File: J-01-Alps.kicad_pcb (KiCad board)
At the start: 2 copper layers, 184 parts, among them SW1 SW_Push, U1 ATmega32U4-AU, U4 PRTR5V0U2X, Y1 16MHz

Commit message: Footprint changes
Changed all of the MX+Alps footprints to Alps only. Also added MX Stabilizer footprints.
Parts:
- removed R6: 10k, Resistor_SMD:R_0603_1608Metric_Pad0.98x0.95mm_HandSolder
- added RC4: 10k, Resistor_SMD:R_0603_1608Metric_Pad0.98x0.95mm_HandSolder, B.Cu at (82.5, 115.0)
- added SW-3800CAPS1: MX_Alps-1.75U, Alps_Only:ALPS-1.5U, F.Cu at (89.7, 113.5)
- added Stab-225U1: Stab-2.25U, MX_Alps_Hybrid:MX-2.25U-Stab-Only, F.Cu at (339.7, 113.5)
- added Stab-225U2: Stab-2.25U, MX_Alps_Hybrid:MX-2.25U-Stab-Only, F.Cu at (96.8, 132.6)
- added Stab-2U1: Stab-2U, MX_Alps_Hybrid:MX-2U-Stab-Only, F.Cu at (342.1, 75.4)
- added Stab-625U1: Stab-6.25U, MX_Alps_Hybrid:MX-6.25U-Stab-Only-Reversed, F.Cu at (206.4, 151.6)
- added Stab-7U1: Stab-7U, MX_Alps_Hybrid:MX-7U-Stab-Only-Reversed, F.Cu at (199.2, 151.6)
- C2, C5, C6, C7, C8, CC1, CC2, D36, D37, D38, D39, D40, D41, D42, D43, D44, D45, D46, D47, D48, D49, D50, D51, D52, D53, D54, D55, D56, D57, D58, D59, D60, D61, D62, D63, D64, D65, D66, D67, D68, D69, D70, D71, D72, D73, D74, D75, D76, D77, D78, D79, D80, F1, JST2, RC1, RC2, RC3, SW1, U1, U4, Y1: moved to B.Cu
- SW-#1, SW-'1, SW-,1, SW--1, SW-.1, SW-/1, SW-0, SW-1, SW-2, SW-3, SW-4, SW-5, SW-6, SW-7, SW-8, SW-9, SW-;1, SW-=1, SW-A1, SW-B1, SW-C1, SW-D1, SW-DEL1, SW-DOWN1, SW-E1, SW-END1, SW-ESC1, SW-F1, SW-G1, SW-H1, SW-I1, SW-J1, SW-K1, SW-L1, SW-LEFT1, SW-M1, SW-M10, SW-M11, SW-M2, SW-M3, SW-M4, SW-M5, SW-M6, SW-M7, SW-M8, SW-M9, SW-N1, SW-O1, SW-P1, SW-PGDN1, SW-PGUP1, SW-Q1, SW-R1, SW-RIGHT1, SW-S1, SW-T1, SW-U1, SW-UP1, SW-V1, SW-W1, SW-X1, SW-Y1, SW-Z1, SW-[1, SW-\1, SW-\3, SW-]1, SW-`1: footprint MX_Alps_Hybrid:MX-1U-NoLED -> Alps_Only:ALPS-1U
- SW-ANSIEN1, SW-LSHIFT1: footprint MX_Alps_Hybrid:MX-2.25U-NoLED -> Alps_Only:ALPS-2.25U
- SW-BKSP1: footprint MX_Alps_Hybrid:MX-2U-NoLED -> Alps_Only:ALPS-2U
- SW-CAPS1, SW-RSHFT1: footprint MX_Alps_Hybrid:MX-1.75U-NoLED -> Alps_Only:ALPS-1.75U
- SW-ISOEN1: footprint MX_Alps_Hybrid:MX-ISO-ReversedStabilizers -> Alps_Only:ALPS-ISO-FLIPPED
- SW-LALT1, SW-LCTRL1, SW-LSHIFT2, SW-LWIN1, SW-STEPCAPS1: footprint MX_Alps_Hybrid:MX-1.25U-NoLED -> Alps_Only:ALPS-1.25U
- SW-LALT2, SW-LCTRL2, SW-RALT1, SW-RCTRL1, SW-TAB1, SW-\2: footprint MX_Alps_Hybrid:MX-1.5U-NoLED -> Alps_Only:ALPS-1.5U
- SW-SPACE625: footprint MX_Alps_Hybrid:MX-6.25U-ReversedStabilizers-NoLED -> Alps_Only:ALPS-6.25U
- SW-SPACE7: footprint MX_Alps_Hybrid:MX-7U-ReversedStabilizers-NoLED -> Alps_Only:ALPS-7U
- moved D70 218.1 mm to (42.9, 154.0), turned to 90 degrees
- moved D52 211.8 mm to (379.4, 115.9), turned to 90 degrees
- moved D71 198.8 mm to (61.9, 154.0), turned to 90 degrees
- moved D51 190.8 mm to (349.2, 114.3), turned to 90 degrees
- moved RC1 181.8 mm to (64.3, 84.1)
- moved RC2 181.4 mm to (64.3, 85.7)
- moved D37 175.9 mm to (60.3, 115.9), turned to 90 degrees
- moved D69 171.5 mm to (379.4, 134.9), turned to 90 degrees
- moved U4 170.9 mm to (70.6, 85.2), turned to 90 degrees
- moved D50 170.4 mm to (333.4, 115.9), turned to 90 degrees
- moved CC1 169.3 mm to (67.5, 93.6), turned to 270 degrees
- moved D72 168.8 mm to (92.1, 154.0), turned to 90 degrees
- moved D36 166.1 mm to (42.9, 115.9), turned to 90 degrees
- moved C2 165.6 mm to (64.3, 111.9), turned to 270 degrees
- moved F1 165.4 mm to (70.6, 80.2)
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
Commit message: Initial routing and additional switch footprints
More bottom row option support (6U, split spacebar), and the start of some column and row routing.
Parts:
- added D75: SOD-123, Diode_SMD:D_SOD-123, B.Cu at (177.0, 154.1)
- added D77: SOD-123, Diode_SMD:D_SOD-123, B.Cu at (269.9, 154.1)
- added SW-LALT3: MX_Alps-1.25U, Alps_Only:ALPS-1.25U, F.Cu at (130.2, 151.6)
- added SW-LALT4: MX_Alps-1.5U, Alps_Only:ALPS-1.5U, F.Cu at (137.3, 151.6)
- added SW-LWIN2: MX_Alps-1U, Alps_Only:ALPS-1U, F.Cu at (108.7, 151.6)
- added SW-LWIN3: MX_Alps-1.U, Alps_Only:ALPS-1U, F.Cu at (113.5, 151.6)
- added SW-MENU1: MX_Alps-1U, Alps_Only:ALPS-1U, F.Cu at (289.7, 151.6)
- added SW-MENU2: MX_Alps-1U, Alps_Only:ALPS-1U, F.Cu at (285.0, 151.6)
- added SW-RALT2: MX_Alps-1.25U, Alps_Only:ALPS-1.25U, F.Cu at (268.3, 151.6)
- added SW-RALT3: MX_Alps-1.5U, Alps_Only:ALPS-1.5U, F.Cu at (261.1, 151.6)
- added SW-RCTRL2: MX_Alps-1.25U, Alps_Only:ALPS-1.25U, F.Cu at (311.1, 151.6)
- added SW-SPACE225: MX_Alps-2.25U, Alps_Only:ALPS-2.25U, F.Cu at (173.0, 151.6)
- added SW-SPACE275: MX_Alps-2.75U, Alps_Only:ALPS-2.75U, F.Cu at (220.7, 151.6)
- added SW-SPACE6: MX_Alps-6U, MX_Alps_Hybrid:MX-6U-Centered-ReversedStabilizers-NoLED, F.Cu at (199.2, 151.6)
- added Stab-225U2: Stab-2.25U, MX_Alps_Hybrid:MX-2.25U-Stab-Only, F.Cu at (173.0, 151.6)
- added Stab-275U1: Stab-2.75U, MX_Alps_Hybrid:MX-2.75U-Stab-Only, F.Cu at (220.7, 151.6)
- moved D79 2.38 mm to (313.5, 154.0)
- moved D72 2.38 mm to (89.7, 154.0)
- moved C2 2.14 mm to (65.2, 110.0)
- moved F1 1.26 mm to (70.0, 81.2)
- moved RC1 1.02 mm to (65.2, 84.5)
- moved RC2 1.00 mm to (65.2, 86.0), turned to 180 degrees
- moved CC1 0.80 mm to (68.3, 93.7)
- moved CC2 0.80 mm to (77.0, 93.7)
- moved C5 0.79 mm to (69.1, 118.3)
- moved C6 0.79 mm to (78.6, 118.3)
- moved C8 0.73 mm to (71.2, 100.5)
- renumbered D75 to D76, D76 to D78, D77 to D79, D78 to D80, D79 to D81, D80 to D82, Stab-225U2 to Stab-225U3
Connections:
- SW-LALT2 pad 1: COL4 -> COL3
- SW-LALT2 pad 2: Net-(D74-Pad2) -> Net-(D73-Pad2)
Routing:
- net ROW0: track 0.00 -> 338.0 mm
- net COL8: track 0.00 -> 106.7 mm
- net COL15: track 0.00 -> 106.4 mm
- net COL3: track 0.00 -> 103.8 mm
- net COL2: track 0.00 -> 103.7 mm
- net D-: track 0.00 -> 100.0 mm, vias 0 -> 2
- net COL12: track 0.00 -> 98.8 mm
- net D+: track 0.00 -> 98.4 mm, vias 0 -> 2
- net COL11: track 0.00 -> 94.8 mm
- net COL13: track 0.00 -> 92.4 mm
- net COL4: track 0.00 -> 91.4 mm
- net COL6: track 0.00 -> 89.0 mm
- net COL16: track 0.00 -> 88.0 mm
- net COL17: track 0.00 -> 80.7 mm
- net COL1: track 0.00 -> 76.2 mm
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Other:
- board outline added: 354 x 96.8 mm
- net class Default: trace_width 0.25 -> 0.254
- net class Power added: clearance 0.2, trace_width 0.381, via_dia 0.8, via_drill 0.4

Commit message: Routing work continued
Most routes placed. Will need to be optimized and cleaned up, but most paths have been figured out.
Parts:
- moved CC2 11.1 mm to (66.0, 95.5), turned to 270 degrees
- moved D74 8.78 mm to (127.8, 154.0)
- moved CC1 5.74 mm to (73.7, 95.5), turned to 90 degrees
- moved D76 4.76 mm to (204.0, 154.0)
- moved Y1 3.35 mm to (69.9, 95.5), turned to 180 degrees
- moved D72 2.56 mm to (92.2, 154.0)
- moved D73 2.24 mm to (115.8, 154.0)
- moved C7 1.85 mm to (81.2, 103.4)
- moved D75 1.51 mm to (175.5, 154.1)
- moved C6 1.15 mm to (78.0, 117.2)
- moved RC3 1.12 mm to (69.6, 134.8)
- moved C5 1.09 mm to (69.5, 117.2)
- moved RC4 1.07 mm to (81.5, 114.8)
- moved D77 0.88 mm to (270.8, 154.1)
- moved D56 0.55 mm to (113.8, 134.9)
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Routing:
- net ROW3: track 0.00 -> 413.8 mm, vias 0 -> 2
- net ROW4: track 0.00 -> 400.9 mm, vias 0 -> 2
- net ROW2: track 0.00 -> 378.7 mm, vias 0 -> 2
- net ROW1: track 0.00 -> 347.2 mm, vias 0 -> 2
- net COL17: track 80.7 -> 388.9 mm
- net COL16: track 88.0 -> 378.4 mm, vias 0 -> 1
- net COL15: track 106.4 -> 385.8 mm
- net COL14: track 64.1 -> 317.6 mm
- net COL13: track 92.4 -> 325.8 mm
- net COL12: track 98.8 -> 312.0 mm
- net COL11: track 94.8 -> 284.0 mm
- net COL10: track 67.0 -> 242.0 mm
- net COL9: track 67.0 -> 222.9 mm
- net COL8: track 106.7 -> 243.8 mm
- net COL7: track 67.0 -> 184.7 mm
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- added copper zone on F.Cu, net +5V
- added copper zone on B.Cu, net GND

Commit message: Continued work on layout
Layout refinements, USB traces, etc.
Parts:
- U4: footprint Package_TO_SOT_SMD:SOT-143 -> random-keyboard-parts:SOT143B
- moved CC2 5.78 mm to (68.9, 90.5), turned to 90 degrees
- moved CC1 5.39 mm to (71.7, 90.5)
- moved JST2 2.77 mm to (75.8, 85.2)
- moved RC3 1.91 mm to (71.5, 134.8), turned to 180 degrees
- moved F1 1.58 mm to (68.5, 81.8)
- moved RC1 1.50 mm to (63.8, 84.5)
- moved RC2 1.50 mm to (63.8, 86.0)
- moved U4 1.50 mm to (69.1, 85.2)
- moved Y1 0.62 mm to (70.3, 95.1)
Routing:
- net +5V: track 29.7 -> 125.2 mm, vias 10 -> 9
- net GND: track 57.0 -> 93.9 mm, vias 0 -> 17
- net ROW4: track 400.9 -> 421.7 mm
- net COL17: track 388.9 -> 408.9 mm
- net COL16: track 378.4 -> 390.7 mm
- net ROW0: track 376.5 -> 385.4 mm, vias 2 -> 0
- net Net-(JST2-Pad2): track 4.61 -> 10.1 mm
- net ROW1: track 347.2 -> 352.6 mm
- net Net-(JST2-Pad3): track 4.73 -> 10.1 mm
- net COL13: track 325.8 -> 330.2 mm
- net COL14: track 317.6 -> 322.0 mm
- net XTAL1: track 11.0 -> 15.3 mm
- net VCC: track 2.93 -> 6.62 mm
- net XTAL2: track 15.5 -> 19.1 mm
- net COL15: track 385.8 -> 389.3 mm
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- added copper zone on F.Cu, net GND
- removed copper zone on F.Cu, net +5V
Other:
- board size 354 x 96.8 mm -> 354.6 x 97.3 mm

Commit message: Verification of routing and dimension
Finished verifying the routing is correct, and the edge-cut dimensions are correct. Double checked the separation between switch areas for Macro columns and arrows / 65% extension keys. Added renders.
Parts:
- moved D69 3.29 mm to (382.7, 134.9)
- moved D18 3.29 mm to (382.7, 77.8)
- moved D35 3.29 mm to (382.7, 96.8)
- moved D52 3.29 mm to (382.7, 115.9)
- moved SW-M1 3.18 mm to (37.3, 75.4)
- moved SW-M3 3.18 mm to (37.3, 94.5)
- moved SW-M5 3.18 mm to (37.3, 113.5)
- moved SW-M2 3.18 mm to (56.4, 75.4)
- moved SW-M4 3.18 mm to (56.4, 94.5)
- moved SW-M6 3.18 mm to (56.4, 113.5)
- moved D2 3.18 mm to (58.7, 77.8)
- moved D20 3.18 mm to (58.7, 96.8)
- moved D54 3.18 mm to (58.7, 134.9)
- moved D71 3.18 mm to (58.7, 154.0)
- moved D1 3.17 mm to (39.7, 77.8)
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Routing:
- net ROW2: track 379.8 -> 389.2 mm
- net ROW3: track 412.8 -> 422.0 mm
- net COL17: track 408.9 -> 402.0 mm
- net ROW4: track 421.7 -> 428.5 mm
- net ROW0: track 385.4 -> 390.4 mm, vias 0 -> 2
- net +5V: track 125.2 -> 120.4 mm
- net XTAL2: track 19.1 -> 15.7 mm
- net COL15: track 389.3 -> 392.2 mm
- net COL1: track 100.0 -> 102.6 mm
- net GND: track 93.9 -> 96.2 mm, vias 17 -> 41
- net COL0: track 110.5 -> 112.5 mm
- net Net-(D17-Pad2): track 8.40 -> 6.83 mm
- net D+: track 100.0 -> 98.5 mm
- net COL16: track 390.7 -> 389.2 mm
- net COL9: track 222.9 -> 224.1 mm
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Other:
- board size 354.6 x 97.3 mm -> 360.1 x 98.9 mm
- board text added: "Alps PCB for J-01 rev1 by robotictomato"
- board text added: "[J]01 Alps"

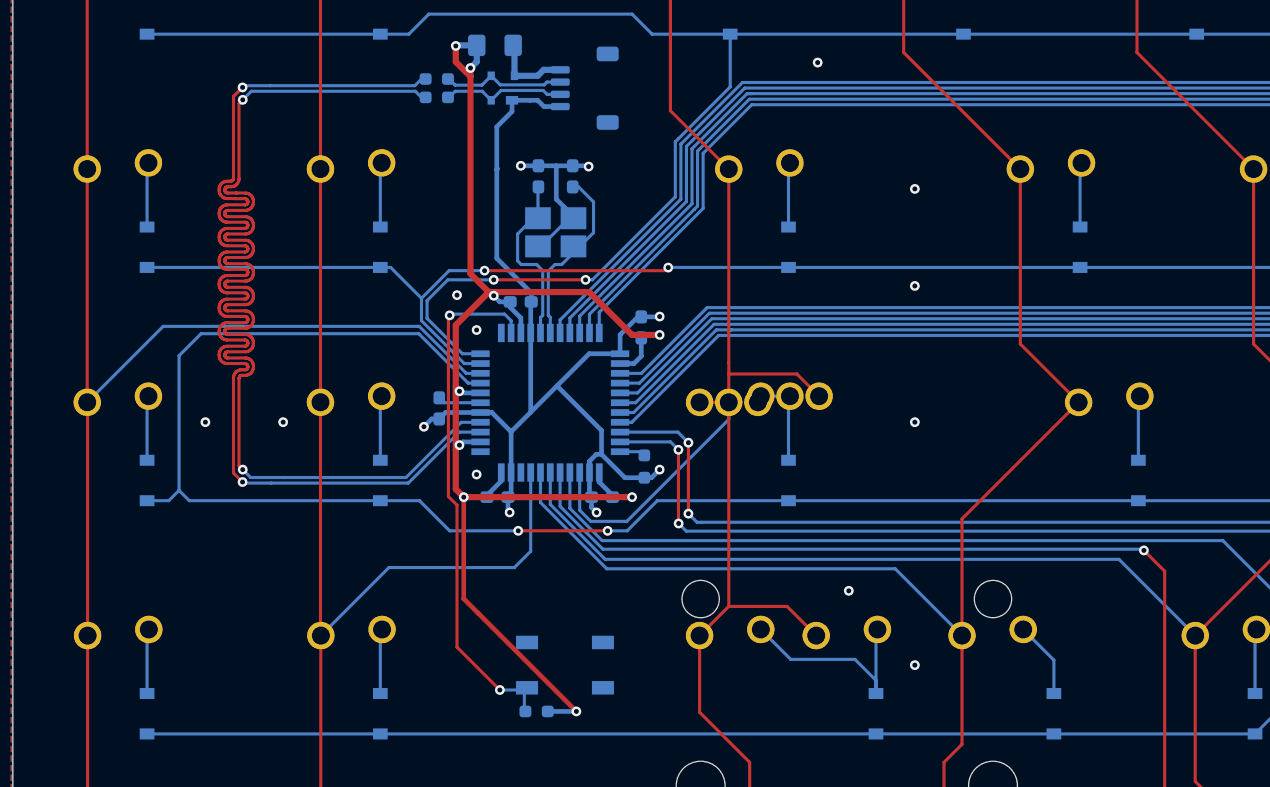
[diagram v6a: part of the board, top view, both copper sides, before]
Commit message: Modifications for QFN footprint
Modifications for ATmega32U4-MU. Rerouting of USB traces, 5V lines, and other supporting components.
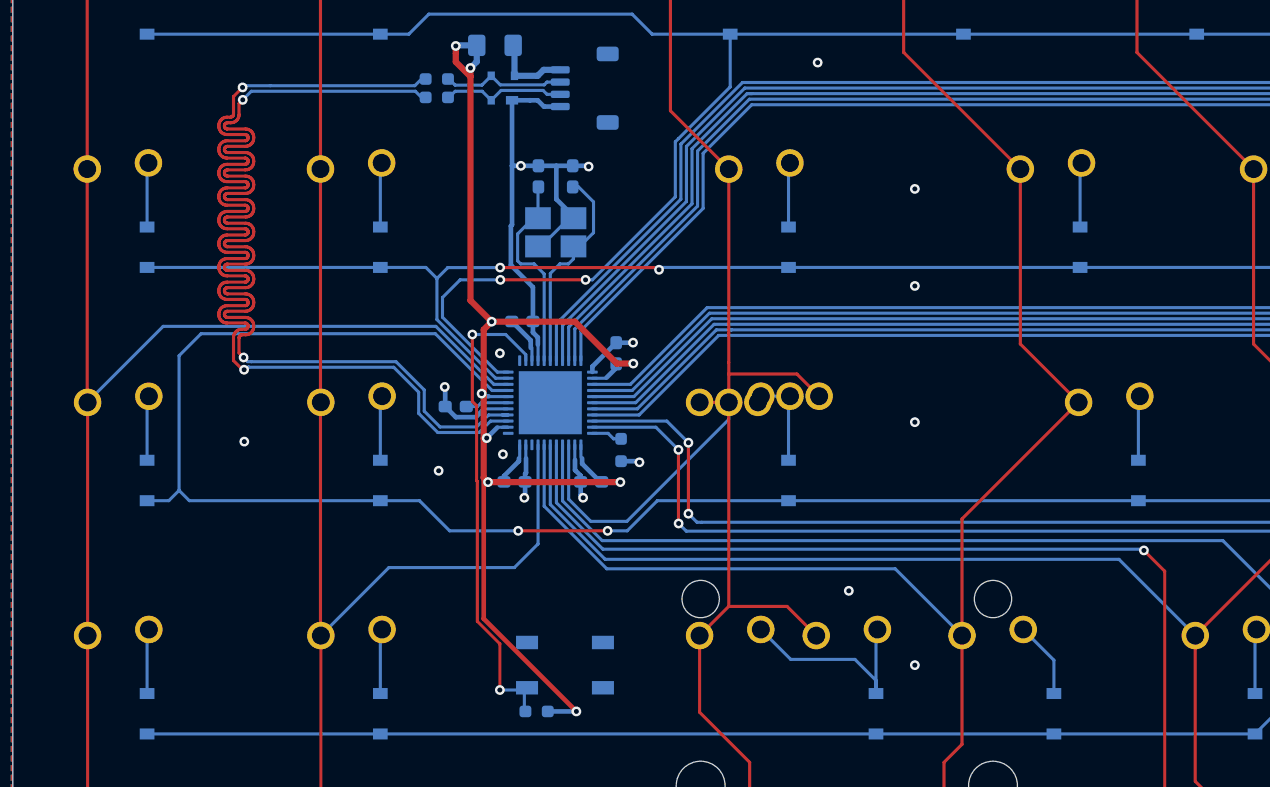
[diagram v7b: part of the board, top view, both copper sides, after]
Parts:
- RC3: value R_Small -> 10k
- U1: value ATmega32U4-AU -> ATmega32U4-MU; footprint Package_QFP:TQFP-44_10x10mm_P0.8mm -> Package_DFN_QFN:QFN-44-1EP_7x7mm_P0.5mm_EP5.15x5.15mm
- moved C7 2.94 mm to (78.0, 105.5)
- moved RC4 2.33 mm to (78.4, 113.4)
- moved C5 1.88 mm to (69.7, 116.0)
- moved C8 1.61 mm to (70.3, 102.9)
- moved C6 1.53 mm to (76.0, 116.0)
- moved C2 1.36 mm to (64.9, 109.8), turned to 180 degrees
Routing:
- net GND: track 96.2 -> 63.7 mm, vias 41 -> 40
- net +5V: track 120.4 -> 115.7 mm
- net Net-(RC3-Pad2): track 43.0 -> 39.8 mm
- net COL13: track 330.8 -> 333.7 mm
- net COL5: track 143.1 -> 145.9 mm
- net COL14: track 322.6 -> 325.4 mm
- net COL0: track 112.5 -> 115.1 mm
- net COL6: track 184.4 -> 187.0 mm
- net COL2: track 124.5 -> 127.1 mm
- net COL12: track 313.2 -> 315.8 mm
- net COL15: track 392.2 -> 394.8 mm
- net ROW3: track 422.0 -> 424.6 mm
- net COL11: track 285.2 -> 287.7 mm
- net COL1: track 102.6 -> 105.2 mm
- net ROW2: track 389.2 -> 391.7 mm
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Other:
- net class MCUPower added: clearance 0.2, trace_width 0.254, via_dia 0.8, via_drill 0.4

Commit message: Additional cleanup
Move to Kicad 6 changes - archive old versions of files.
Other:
- net class Default removed
- net class MCUPower removed
- net class Power removed
